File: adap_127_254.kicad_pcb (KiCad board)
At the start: 2 copper layers, 2 parts, among them J1 Conn_02x05_Odd_Even, J2 Conn_02x05_Odd_Even

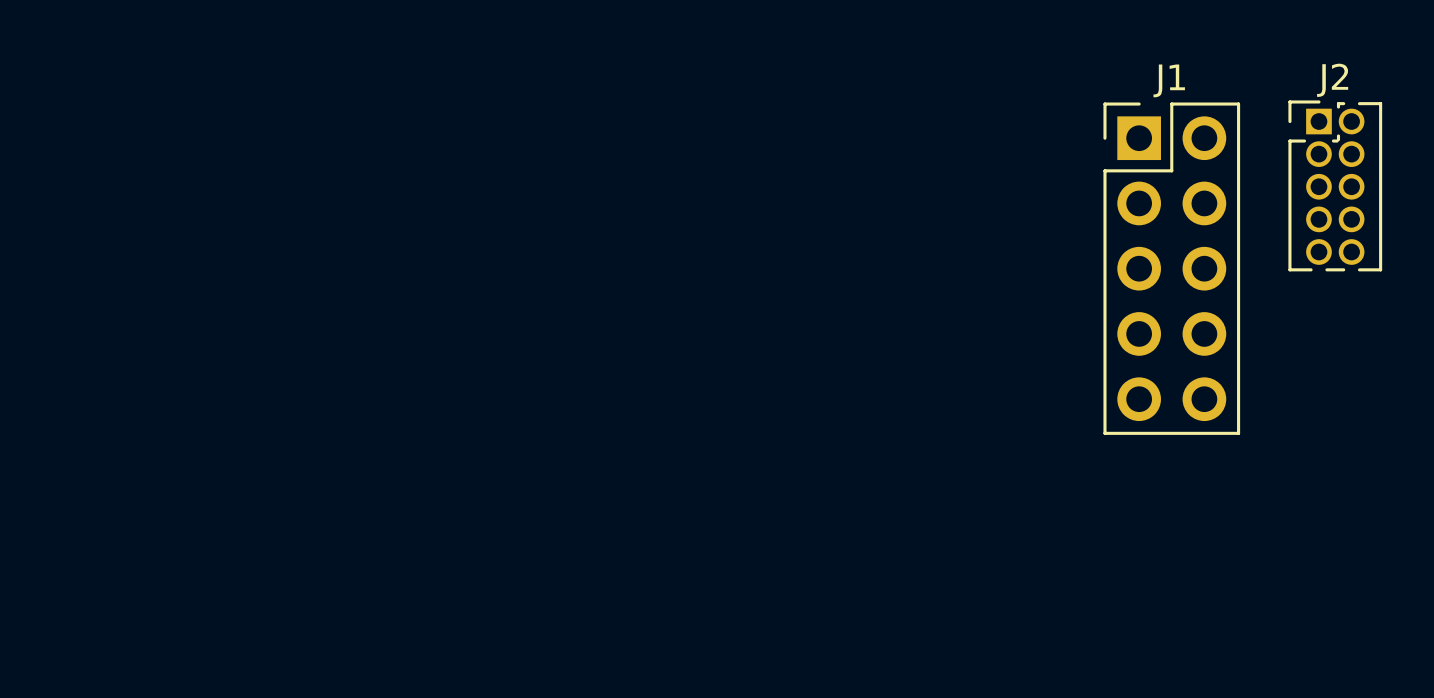
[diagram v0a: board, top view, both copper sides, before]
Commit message: pcb edge cutos - components placed in final place
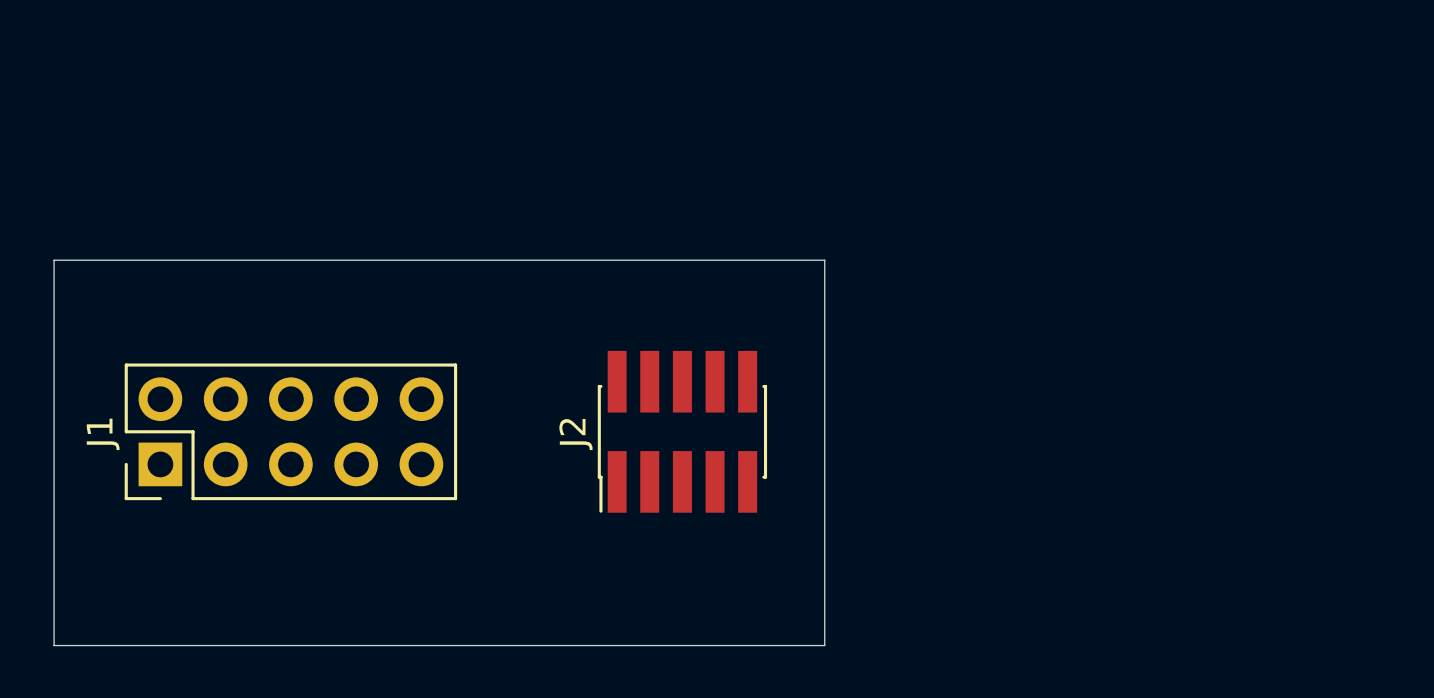
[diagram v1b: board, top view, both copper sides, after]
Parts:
- J2: footprint Connector_PinHeader_1.27mm:PinHeader_2x05_P1.27mm_Vertical -> Connector_PinHeader_1.27mm:PinHeader_2x05_P1.27mm_Vertical_SMD
- moved J1 40.2 mm to (104.1, 108.0), turned to 90 degrees
- moved J2 27.6 mm to (124.5, 106.7), turned to 90 degrees
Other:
- board outline added: 30 x 15 mm

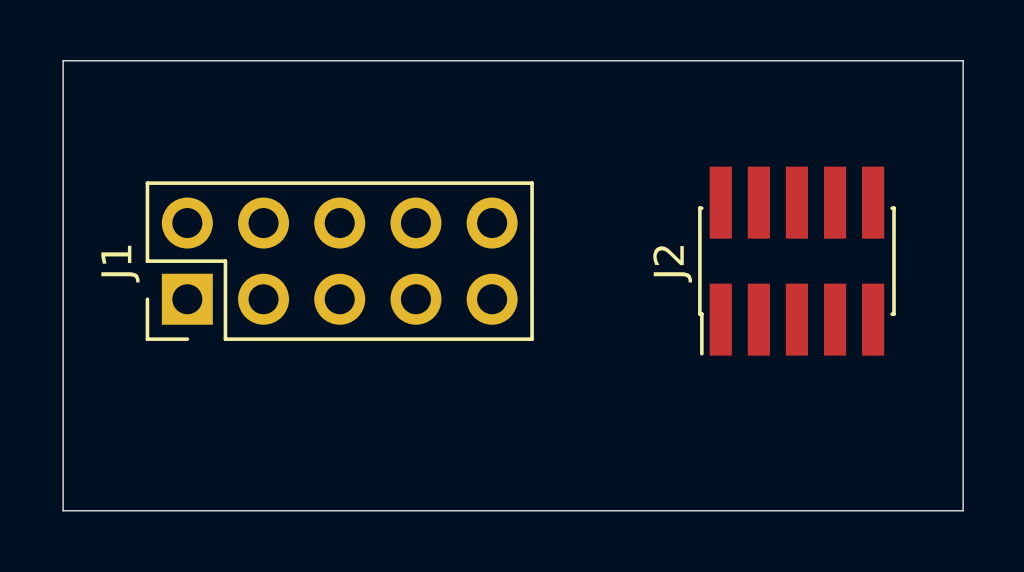
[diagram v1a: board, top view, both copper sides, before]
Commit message: pcb finished routing
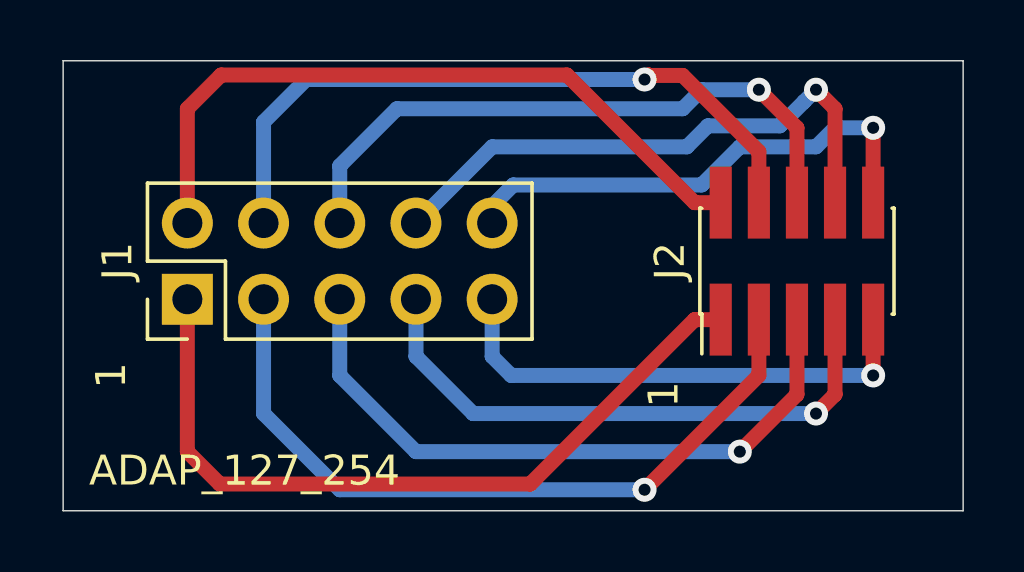
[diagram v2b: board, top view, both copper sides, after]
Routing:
- net Net-(J1-Pad1): track 0.00 -> 25.6 mm
- net Net-(J1-Pad3): track 0.00 -> 24.8 mm, vias 0 -> 1
- net Net-(J1-Pad2): track 0.00 -> 23.8 mm
- net Net-(J1-Pad4): track 0.00 -> 23.3 mm, vias 0 -> 1
- net Net-(J1-Pad5): track 0.00 -> 22.1 mm, vias 0 -> 1
- net Net-(J1-Pad6): track 0.00 -> 21.2 mm, vias 0 -> 1
- net Net-(J1-Pad7): track 0.00 -> 19.4 mm, vias 0 -> 1
- net Net-(J1-Pad8): track 0.00 -> 19.2 mm, vias 0 -> 1
- net Net-(J1-Pad10): track 0.00 -> 16.8 mm, vias 0 -> 1
- net Net-(J1-Pad9): track 0.00 -> 16.7 mm, vias 0 -> 1
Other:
- net class Default: trace_width 0.25 -> 0.5
- board text added: "1"
- board text added: "ADAP_127_254"
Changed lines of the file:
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@@
   (general
     (thickness 1.6)
-    (drawings 4)
-    (tracks 0)
+    (drawings 8)
+    (tracks 69)
     (zones 0)
     (modules 2)
@@
   )
   (setup
-    (last_trace_width 0.25)
+    (last_trace_width 0.5)
     (trace_clearance 0.2)
     (zone_clearance 0.508)
@@
   (net_class Default "This is the default net class."
     (clearance 0.2)
-    (trace_width 0.25)
+    (trace_width 0.5)
     (via_dia 0.8)
     (via_drill 0.4)
@@
     )
   )
+  (gr_text ADAP_127_254 (at 106.045 113.665) (layer B.SilkS)
+    (effects (font (size 1 1) (thickness 0.15)) (justify mirror))
+  )
+  (gr_text ADAP_127_254 (at 106.045 113.665) (layer F.SilkS)
+    (effects (font (size 1 1) (thickness 0.15)))
+  )
+  (gr_text 1 (at 120.015 111.125 90) (layer F.SilkS)
+    (effects (font (size 1 1) (thickness 0.15)))
+  )
+  (gr_text 1 (at 101.6 110.49 90) (layer F.SilkS)
+    (effects (font (size 1 1) (thickness 0.15)))
+  )
   (gr_line (start 100 115) (end 130 115) (layer Edge.Cuts) (width 0.05))
   (gr_line (start 100 100) (end 130 100) (layer Edge.Cuts) (width 0.05))
   (gr_line (start 130 100) (end 130 115) (layer Edge.Cuts) (width 0.05))
   (gr_line (start 100 100) (end 100 115) (layer Edge.Cuts) (width 0.05))
+  (segment (start 127 104.73) (end 127 102.235) (width 0.5) (layer F.Cu) (net 1))
+  (via (at 127 102.235) (size 0.8) (drill 0.4) (layers F.Cu B.Cu) (net 1))
+  (segment (start 125.73 102.235) (end 127 102.235) (width 0.5) (layer B.Cu) (net 1))
+  (segment (start 125.095 102.87) (end 125.73 102.235) (width 0.5) (layer B.Cu) (net 1))
+  (segment (start 122.555 102.87) (end 125.095 102.87) (width 0.5) (layer B.Cu) (net 1))
+  (segment (start 121.285 104.14) (end 122.555 102.87) (width 0.5) (layer B.Cu) (net 1))
+  (segment (start 115.002919 104.14) (end 121.285 104.14) (width 0.5) (layer B.Cu) (net 1))
+  (segment (start 114.3 104.842919) (end 115.002919 104.14) (width 0.5) (layer B.Cu) (net 1))
+  (segment (start 114.3 105.41) (end 114.3 104.842919) (width 0.5) (layer B.Cu) (net 1))
+  (segment (start 127 108.63) (end 127 110.49) (width 0.5) (layer F.Cu) (net 2))
+  (via (at 127 110.49) (size 0.8) (drill 0.4) (layers F.Cu B.Cu) (net 2))
+  (segment (start 127 110.49) (end 114.935 110.49) (width 0.5) (layer B.Cu) (net 2))
+  (segment (start 114.3 109.855) (end 114.3 107.95) (width 0.5) (layer B.Cu) (net 2))
+  (segment (start 114.935 110.49) (end 114.3 109.855) (width 0.5) (layer B.Cu) (net 2))
+  (segment (start 125.73 104.73) (end 125.73 101.6) (width 0.5) (layer F.Cu) (net 3))
+  (segment (start 125.73 101.6) (end 125.095 100.965) (width 0.5) (layer F.Cu) (net 3))
+  (via (at 125.095 100.965) (size 0.8) (drill 0.4) (layers F.Cu B.Cu) (net 3))
+  (segment (start 123.890011 102.169989) (end 124.695001 101.364999) (width 0.5) (layer B.Cu) (net 3))
+  (segment (start 120.790017 102.87) (end 121.490028 102.169989) (width 0.5) (layer B.Cu) (net 3))
+  (segment (start 124.695001 101.364999) (end 125.095 100.965) (width 0.5) (layer B.Cu) (net 3))
+  (segment (start 111.76 105.41) (end 114.3 102.87) (width 0.5) (layer B.Cu) (net 3))
+  (segment (start 121.490028 102.169989) (end 123.890011 102.169989) (width 0.5) (layer B.Cu) (net 3))
+  (segment (start 114.3 102.87) (end 120.790017 102.87) (width 0.5) (layer B.Cu) (net 3))
+  (segment (start 111.76 107.95) (end 111.76 109.855) (width 0.5) (layer B.Cu) (net 4))
+  (segment (start 111.76 109.855) (end 113.665 111.76) (width 0.5) (layer B.Cu) (net 4))
+  (segment (start 113.665 111.76) (end 125.095 111.76) (width 0.5) (layer B.Cu) (net 4))
+  (via (at 125.095 111.76) (size 0.8) (drill 0.4) (layers F.Cu B.Cu) (net 4))
+  (segment (start 125.095 111.76) (end 125.73 111.125) (width 0.5) (layer F.Cu) (net 4))
+  (segment (start 125.73 111.125) (end 125.73 108.63) (width 0.5) (layer F.Cu) (net 4))
+  (segment (start 124.46 104.73) (end 124.46 102.235) (width 0.5) (layer F.Cu) (net 5))
+  (segment (start 124.46 102.235) (end 123.19 100.965) (width 0.5) (layer F.Cu) (net 5))
+  (via (at 123.19 100.965) (size 0.8) (drill 0.4) (layers F.Cu B.Cu) (net 5))
+  (segment (start 109.22 103.505) (end 109.22 105.41) (width 0.5) (layer B.Cu) (net 5))
+  (segment (start 111.125 101.6) (end 109.22 103.505) (width 0.5) (layer B.Cu) (net 5))
+  (segment (start 120.65 101.6) (end 111.125 101.6) (width 0.5) (layer B.Cu) (net 5))
+  (segment (start 123.19 100.965) (end 121.285 100.965) (width 0.5) (layer B.Cu) (net 5))
+  (segment (start 121.285 100.965) (end 120.65 101.6) (width 0.5) (layer B.Cu) (net 5))
+  (via (at 122.555 113.03) (size 0.8) (drill 0.4) (layers F.Cu B.Cu) (net 6))
+  (segment (start 122.555 113.03) (end 124.46 111.125) (width 0.5) (layer F.Cu) (net 6))
+  (segment (start 124.46 111.125) (end 124.46 108.63) (width 0.5) (layer F.Cu) (net 6))
+  (segment (start 111.76 113.03) (end 122.555 113.03) (width 0.5) (layer B.Cu) (net 6))
+  (segment (start 109.22 107.95) (end 109.22 110.49) (width 0.5) (layer B.Cu) (net 6))
+  (segment (start 109.22 110.49) (end 111.76 113.03) (width 0.5) (layer B.Cu) (net 6))
+  (segment (start 123.19 103.03) (end 120.65 100.49) (width 0.5) (layer F.Cu) (net 7))
+  (segment (start 123.19 104.73) (end 123.19 103.03) (width 0.5) (layer F.Cu) (net 7))
+  (segment (start 119.54 100.49) (end 119.52501 100.47501) (width 0.5) (layer F.Cu) (net 7))
+  (segment (start 120.65 100.49) (end 119.54 100.49) (width 0.5) (layer F.Cu) (net 7))
+  (via (at 119.38 100.625) (size 0.8) (drill 0.4) (layers F.Cu B.Cu) (net 7))
+  (segment (start 119.52501 100.47501) (end 119.52501 100.47999) (width 0.5) (layer F.Cu) (net 7))
+  (segment (start 119.52501 100.47999) (end 119.38 100.625) (width 0.5) (layer F.Cu) (net 7))
+  (segment (start 119.38 100.625) (end 108.09999 100.625) (width 0.5) (layer B.Cu) (net 7))
+  (segment (start 106.68 102.04499) (end 106.68 105.41) (width 0.5) (layer B.Cu) (net 7))
+  (segment (start 108.09999 100.625) (end 106.68 102.04499) (width 0.5) (layer B.Cu) (net 7))
+  (via (at 119.38 114.3) (size 0.8) (drill 0.4) (layers F.Cu B.Cu) (net 8))
+  (segment (start 123.19 110.49) (end 123.19 108.63) (width 0.5) (layer F.Cu) (net 8))
+  (segment (start 119.38 114.3) (end 123.19 110.49) (width 0.5) (layer F.Cu) (net 8))
+  (segment (start 106.68 111.76) (end 106.68 107.95) (width 0.5) (layer B.Cu) (net 8))
+  (segment (start 119.38 114.3) (end 109.22 114.3) (width 0.5) (layer B.Cu) (net 8))
+  (segment (start 109.22 114.3) (end 106.68 111.76) (width 0.5) (layer B.Cu) (net 8))
+  (segment (start 104.14 101.6) (end 104.14 105.41) (width 0.5) (layer F.Cu) (net 9))
+  (segment (start 105.26499 100.47501) (end 104.14 101.6) (width 0.5) (layer F.Cu) (net 9))
+  (segment (start 116.79501 100.47501) (end 105.26499 100.47501) (width 0.5) (layer F.Cu) (net 9))
+  (segment (start 121.92 104.73) (end 121.05 104.73) (width 0.5) (layer F.Cu) (net 9))
+  (segment (start 121.05 104.73) (end 116.79501 100.47501) (width 0.5) (layer F.Cu) (net 9))
+  (segment (start 121.05 108.63) (end 115.57 114.11) (width 0.5) (layer F.Cu) (net 10))
+  (segment (start 121.92 108.63) (end 121.05 108.63) (width 0.5) (layer F.Cu) (net 10))
+  (segment (start 115.57 114.11) (end 105.22 114.11) (width 0.5) (layer F.Cu) (net 10))
+  (segment (start 104.14 113.03) (end 104.14 107.95) (width 0.5) (layer F.Cu) (net 10))
+  (segment (start 105.22 114.11) (end 104.14 113.03) (width 0.5) (layer F.Cu) (net 10))
 )

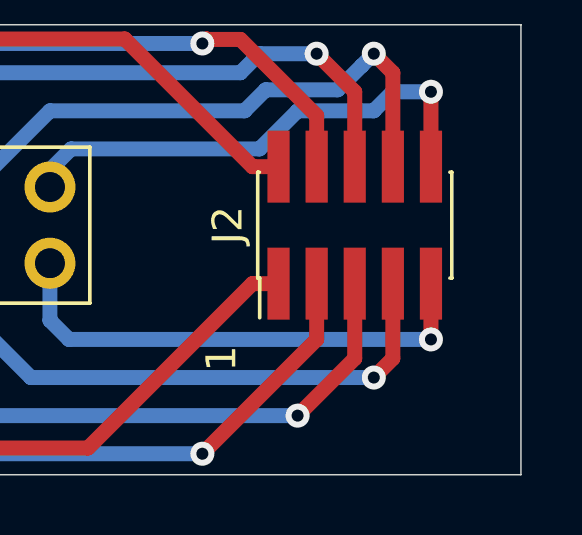
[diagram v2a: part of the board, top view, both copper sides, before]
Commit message: add OSHW logo to pcb - single board gerber files created
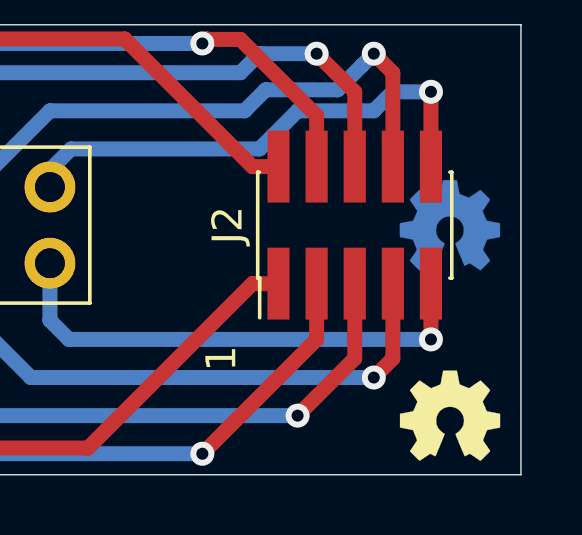
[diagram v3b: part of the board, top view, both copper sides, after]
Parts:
- added REF**: OSHW-Symbol_3.3x3mm_Copper, Symbol:OSHW-Symbol_3.3x3mm_Copper, B.Cu at (127.6, 106.7)
- added REF**: OSHW-Symbol_3.3x3mm_SilkScreen, Symbol:OSHW-Symbol_3.3x3mm_SilkScreen, F.Cu at (127.6, 113.0)
